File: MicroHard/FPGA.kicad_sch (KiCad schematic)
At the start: 1 part, among them SW3 KMR221NGLFS

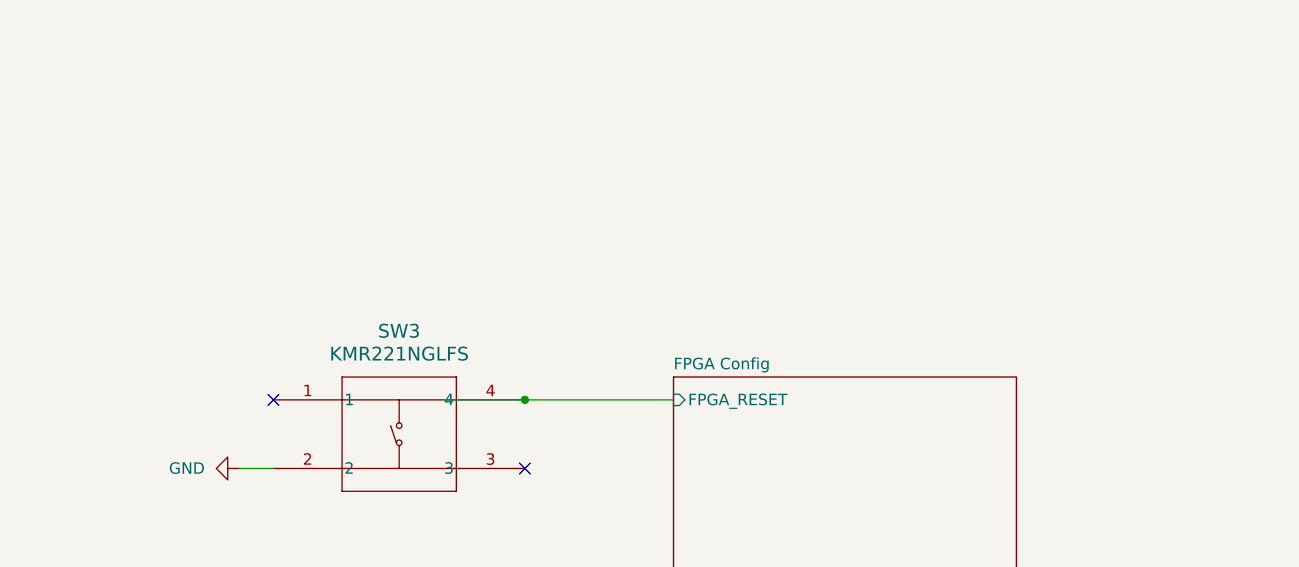
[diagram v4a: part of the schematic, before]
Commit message: feat: VGA out lines from FPGA drawn
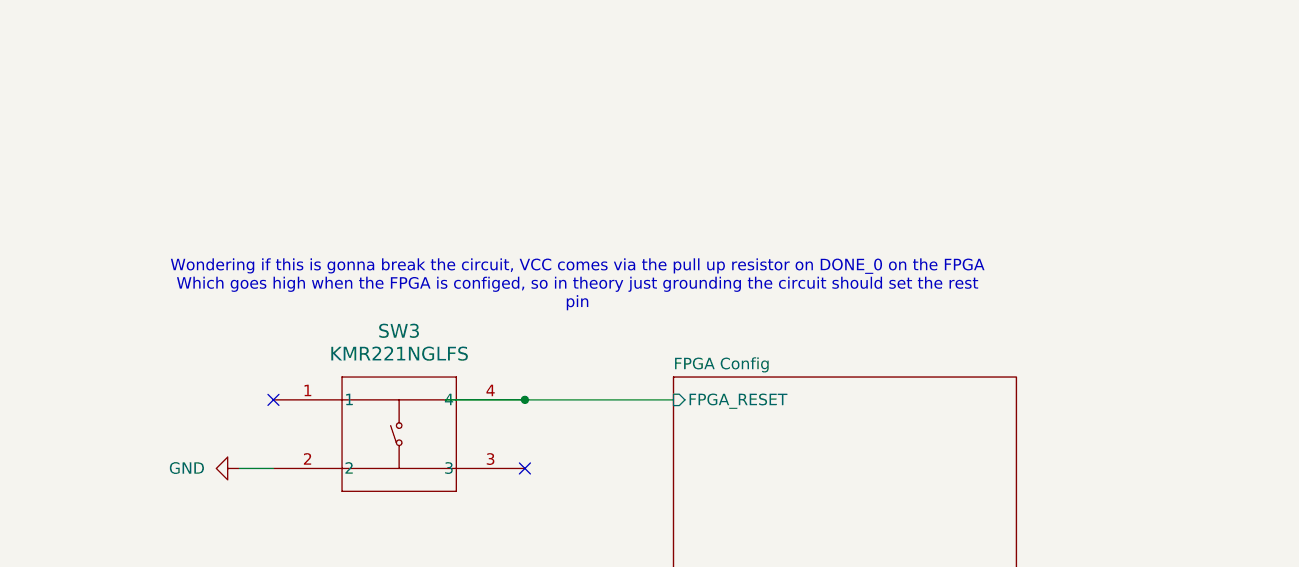
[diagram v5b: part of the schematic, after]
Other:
- note added: "Wondering if this is gonna break the circuit, VCC comes via the pull up resistor on DONE_0 on the FPGA Which goes high when the FPGA is configed, so in theory just grounding the circuit should set the rest pin"
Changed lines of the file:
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@@
+		)
+	)
+	(text "Wondering if this is gonna break the circuit, VCC comes via the pull up resistor on DONE_0 on the FPGA\nWhich goes high when the FPGA is configed, so in theory just grounding the circuit should set the rest \npin\n"
+		(exclude_from_sim no)
+		(at 69.342 101.6 0)
+		(effects
+			(font
+				(size 1.27 1.27)
+			)
 		)
 	)
@@
 		(dnp no)
 		(fields_autoplaced yes)
-		(property "Reference" "#PWR030"
+		(property "Reference" "#PWR021"
 			(at 25.4 121.92 0)
 			(effects
@@
 			(project ""
 				(path "/578bd531-a491-4b15-a479-460d159ffc14/e381883e-e672-4900-88a5-08b94f970a88"
-					(reference "#PWR030")
+					(reference "#PWR021")
 					(unit 1)
 				)

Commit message: feat: finished schematic, TODO: go through checklist
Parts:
- SW3: footprint KMR221_CNK -> (none)
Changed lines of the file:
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@@
 			)
 		)
-		(property "Footprint" "KMR221_CNK"
+		(property "Footprint" ""
 			(at 35.56 114.3 0)
 			(effects

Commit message: feat: completed schematic draft
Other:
- sheet FPGA Config ports: added none; removed FPGA_CONFIG_CLOCK
- sheet Unit A ports: added none; removed FPGA_CONFIG_CLOCK
- note removed: "Wondering if this is gonna break the circuit, VCC comes via the pull up resistor on DONE_0 on the FPGA Which goes high when the FPGA is configed, so in theory just grounding the circuit should set the rest pin"
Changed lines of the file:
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@@
-	(wire
-		(pts
-			(xy 118.11 147.32) (xy 205.74 147.32)
-		)
-		(stroke
-			(width 0)
-			(type default)
-		)
-	)
 	(wire
 		(pts
@@
 			(width 0)
 			(type default)
-		)
-	)
-	(text "Wondering if this is gonna break the circuit, VCC comes via the pull up resistor on DONE_0 on the FPGA\nWhich goes high when the FPGA is configed, so in theory just grounding the circuit should set the rest \npin\n"
-		(exclude_from_sim no)
-		(at 69.342 101.6 0)
-		(effects
-			(font
-				(size 1.27 1.27)
-			)
 		)
 	)
@@
 			)
 		)
-		(pin "FPGA_CONFIG_CLOCK" input
-			(at 205.74 147.32 180)
-			(effects
-				(font
-					(size 1.27 1.27)
-				)
-				(justify left)
-			)
-		)
 		(instances
 			(project "MicroHard"
@@
 			)
 		)
-		(pin "FPGA_CONFIG_CLOCK" input
-			(at 118.11 147.32 0)
-			(effects
-				(font
-					(size 1.27 1.27)
-				)
-				(justify right)
-			)
-		)

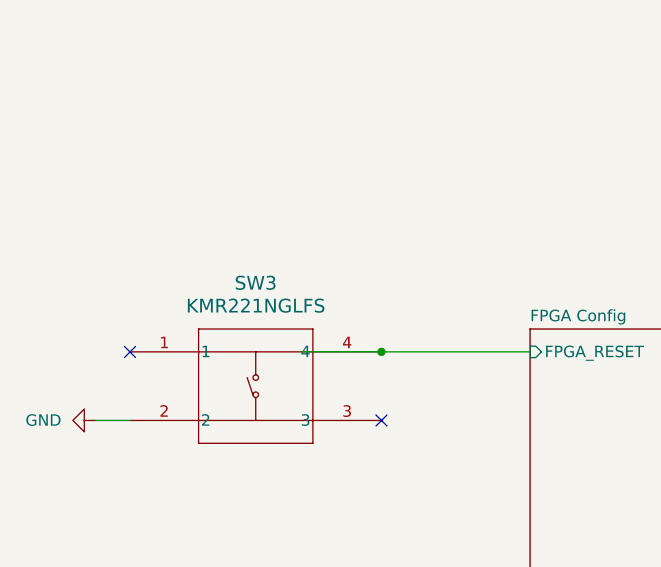
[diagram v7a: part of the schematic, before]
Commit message: Renumber parts
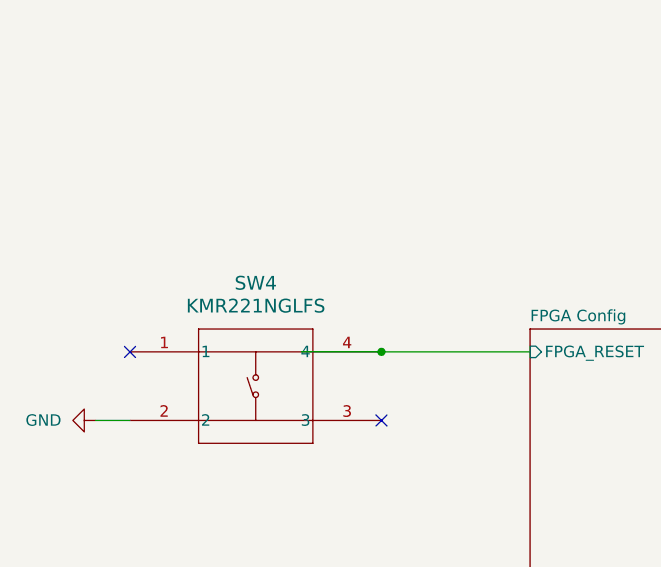
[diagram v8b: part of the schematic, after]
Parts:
- renumbered SW3 to SW4
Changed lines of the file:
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@@
 		(dnp no)
 		(fields_autoplaced yes)
-		(property "Reference" "SW3"
+		(property "Reference" "SW4"
 			(at 49.53 106.68 0)
 			(effects
@@
 			(project "MicroHard"
 				(path "/578bd531-a491-4b15-a479-460d159ffc14/e381883e-e672-4900-88a5-08b94f970a88"
-					(reference "SW3")
+					(reference "SW4")
 					(unit 1)
 				)
@@
 		(dnp no)
 		(fields_autoplaced yes)
-		(property "Reference" "#PWR021"
+		(property "Reference" "#PWR027"
 			(at 25.4 121.92 0)
 			(effects
@@
 			(project ""
 				(path "/578bd531-a491-4b15-a479-460d159ffc14/e381883e-e672-4900-88a5-08b94f970a88"
-					(reference "#PWR021")
+					(reference "#PWR027")
 					(unit 1)
 				)
